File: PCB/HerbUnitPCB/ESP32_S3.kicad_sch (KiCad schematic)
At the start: 12 parts, among them J1 USB_C_Receptacle_USB2.0_16P, U1 USBLC6-2P6, U2 AP2112K-3.3, U3 ESP32-S3-MINI-1

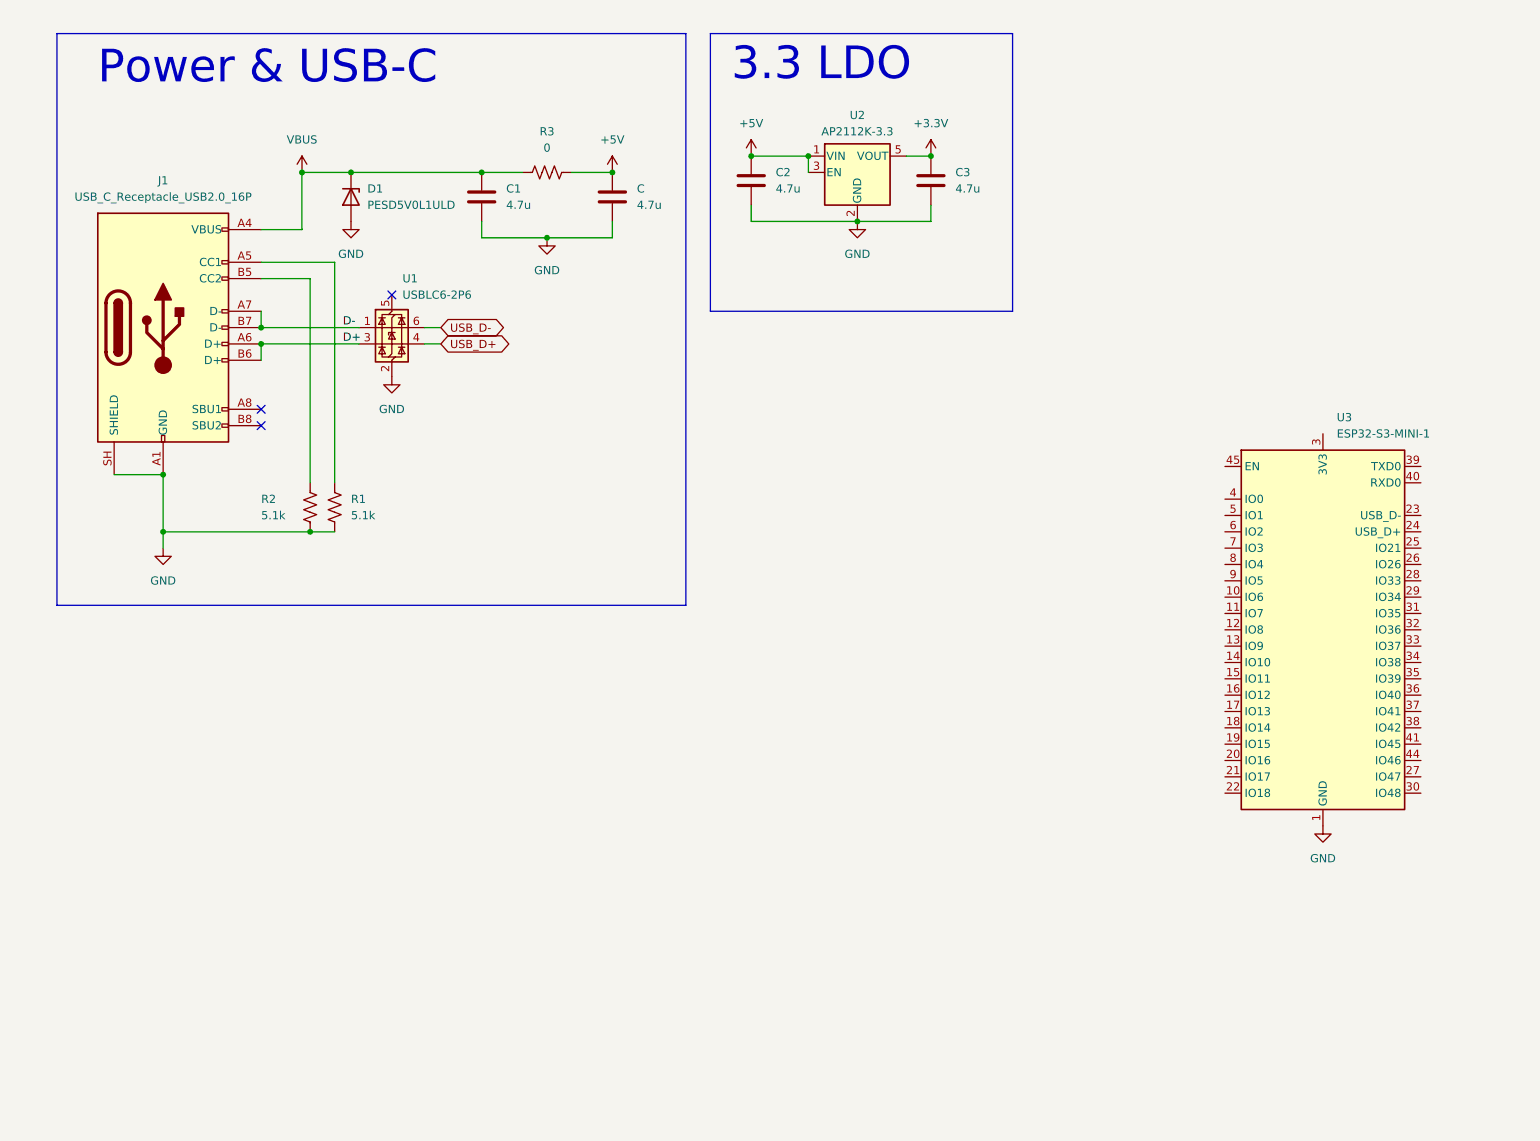
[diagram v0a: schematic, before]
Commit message: Schematic Progress
- Finished ESP Schematic
- Began Peripherals Schematic
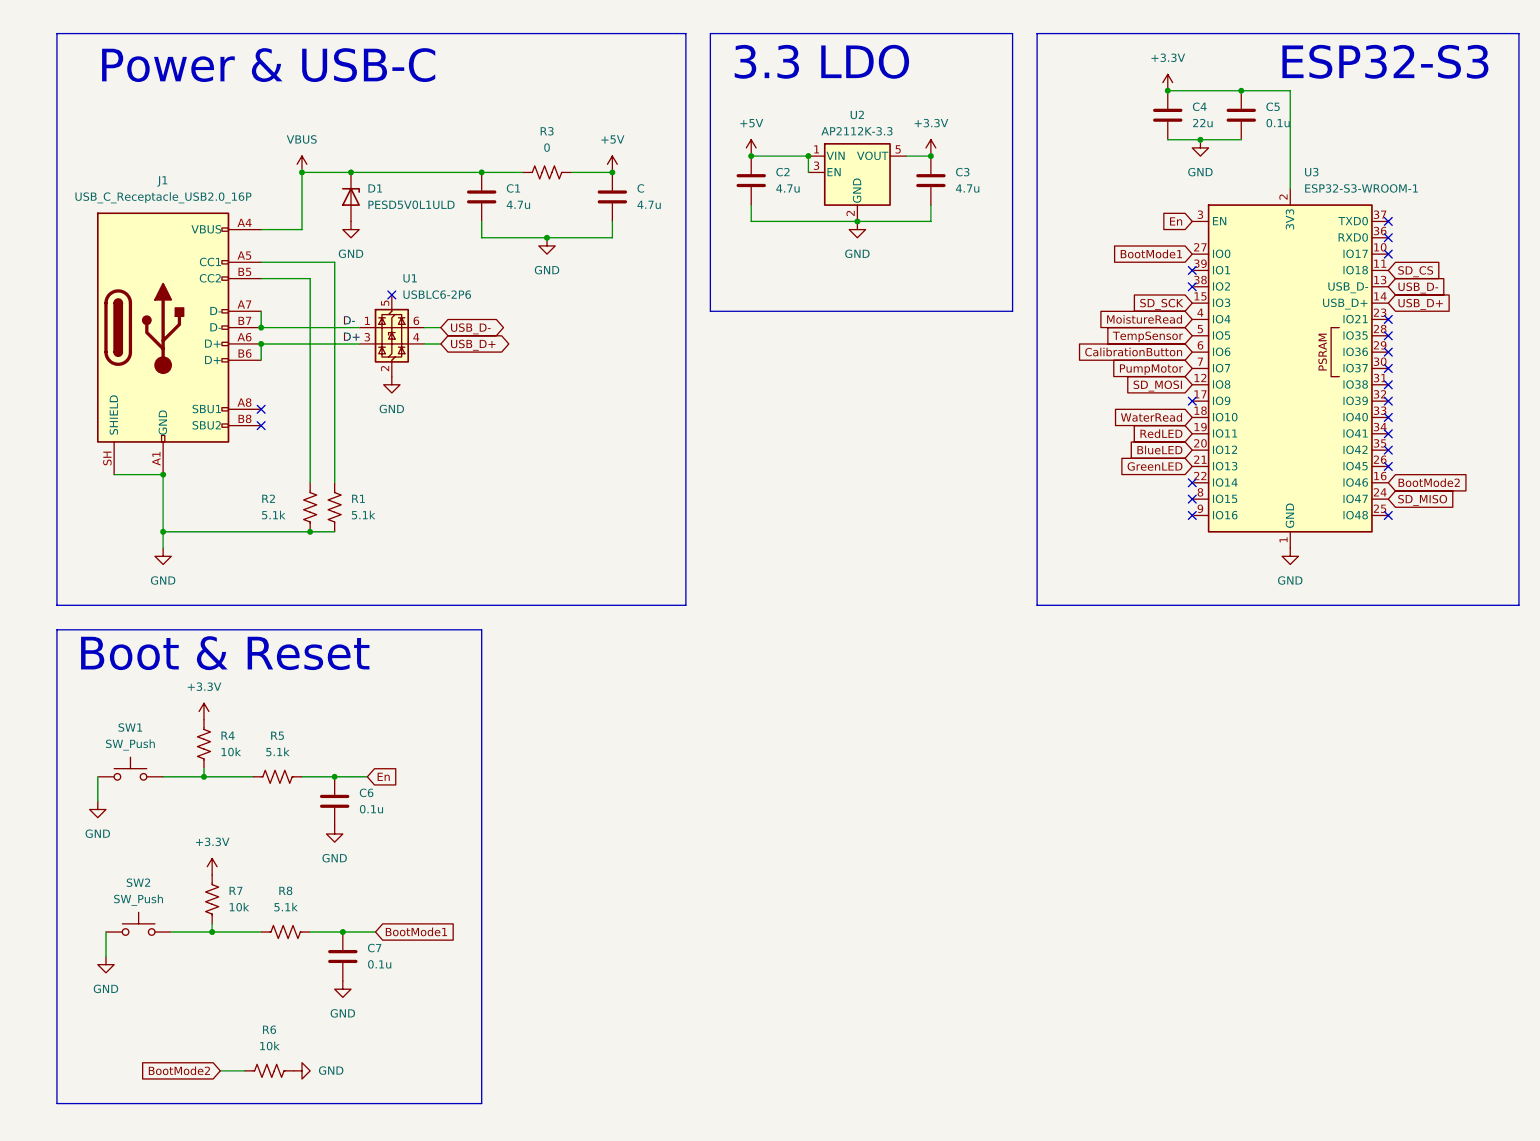
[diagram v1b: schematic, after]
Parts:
- removed U3: ESP32-S3-MINI-1, RF_Module:ESP32-S2-MINI-1, symbol RF_Module:ESP32-S3-MINI-1
- added C4: 22u, Capacitor_SMD:C_0402_1005Metric, symbol Device:C
- added C5, C6, C7: 0.1u, Capacitor_SMD:C_0402_1005Metric, symbol Device:C
- added R4, R6, R7: 10k, Resistor_SMD:R_0402_1005Metric, symbol Device:R_US
- added R5, R8: 5.1k, Resistor_SMD:R_0402_1005Metric, symbol Device:R_US
- added SW1, SW2: SW_Push, Button_Switch_SMD:SW_SPST_B3U-1000P, symbol Switch:SW_Push
- added U3: ESP32-S3-WROOM-1, RF_Module:ESP32-S3-WROOM-1, symbol RF_Module:ESP32-S3-WROOM-1
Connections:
- net +3.3V: now also C4.1, C5.1, R4.1, R7.1, U3.2 (3V3)
- net GND: now also C4.2, C5.2, C6.2, C7.2, R6.2, SW1.1, SW2.1, U3.1 (GND), U3.40 (GND), U3.41 (GND)
- net USB_D+: now also U3.14 (USB_D+)
- net USB_D-: now also U3.13 (USB_D-)
- new net: R7.2, R8.1, SW2.2
- new net: R4.2, R5.1, SW1.2
- new net BlueLED: U3.20 (IO12)
- new net BootMode1: C7.1, R8.2, U3.27 (IO0)
- new net BootMode2: R6.1, U3.16 (IO46)
- new net CalibrationButton: U3.6 (IO6)
- new net En: C6.1, R5.2, U3.3 (EN)
- new net GreenLED: U3.21 (IO13)
- new net MoistureRead: U3.4 (IO4)
- new net PumpMotor: U3.7 (IO7)
- new net RedLED: U3.19 (IO11)
- new net SD_CS: U3.11 (IO18)
- new net SD_MISO: U3.24 (IO47)
- new net SD_MOSI: U3.12 (IO8)
- new net SD_SCK: U3.15 (IO3)
- new net TempSensor: U3.5 (IO5)
- new net WaterRead: U3.18 (IO10)
- no-connect marks 3 -> 23
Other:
- note added: "Boot & Reset"
- note added: "ESP32-S3"

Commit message: Peripherals
Finished most of the Peripherals.
- Added temp sensor
- Added Moisture sensor
- Added float switch
- Added SD card reader/writer
- Still need to add barrel jack/pump
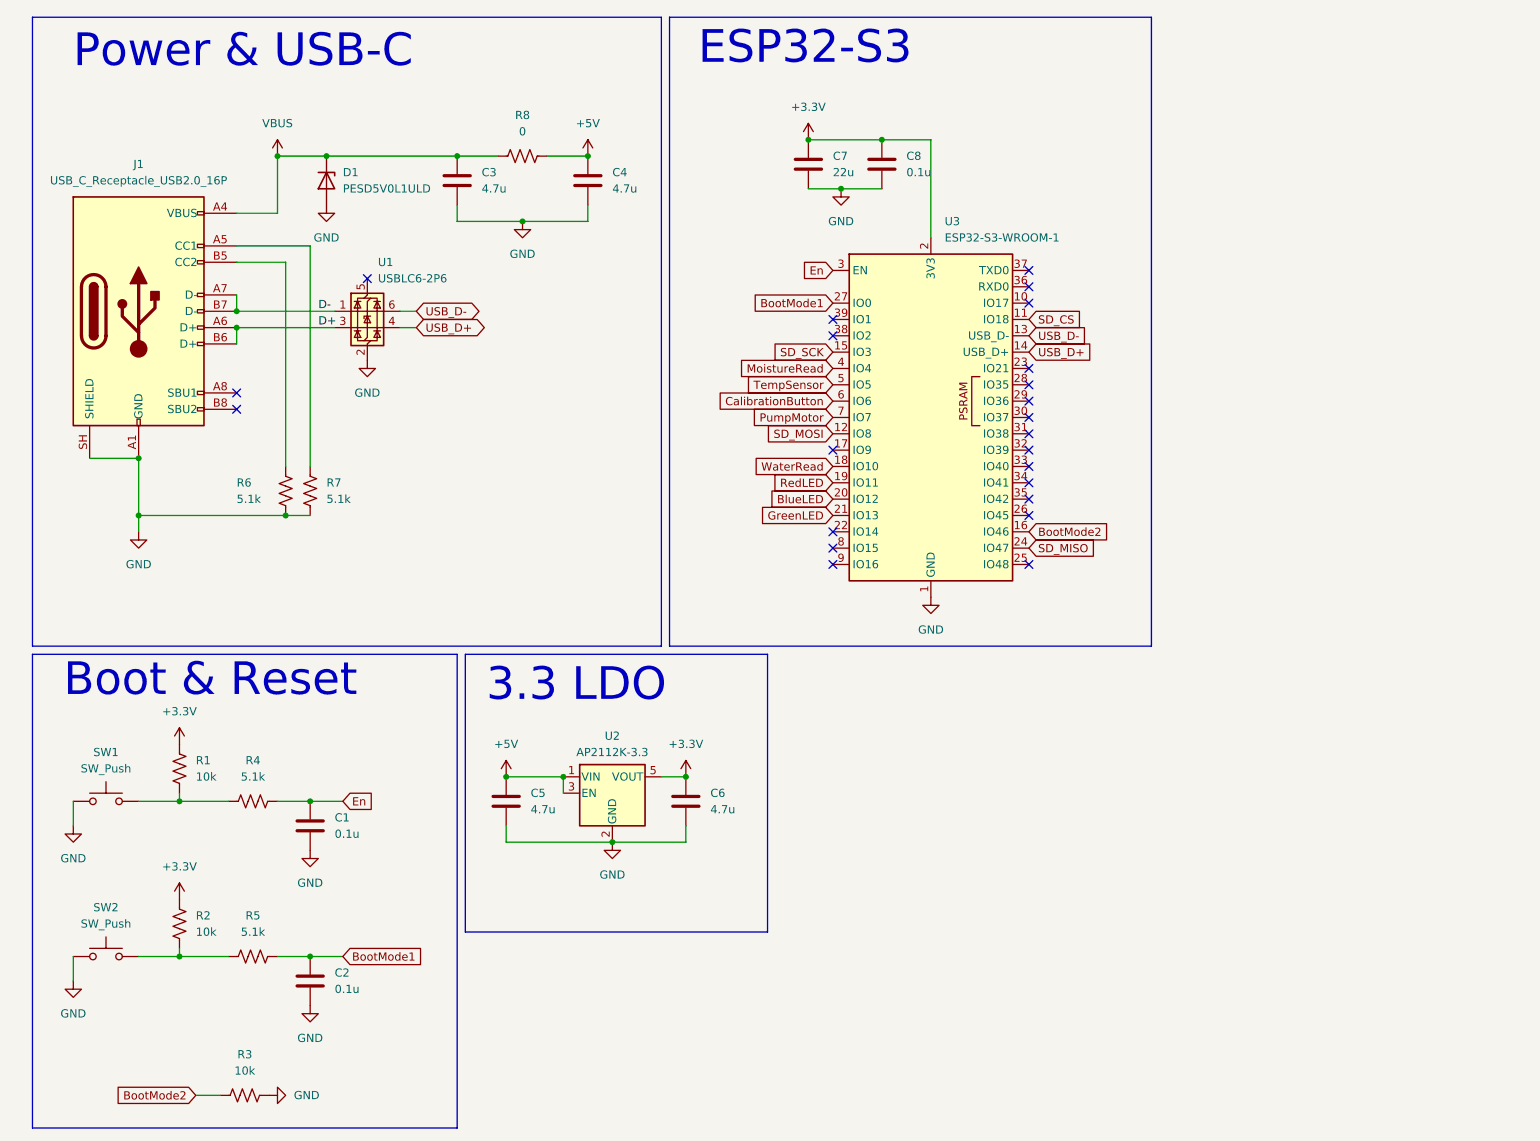
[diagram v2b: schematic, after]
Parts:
- renumbered C6 to C1, C7 to C2, C1 to C3, C to C4, C2 to C5, C3 to C6, C4 to C7, C5 to C8, R4 to R1, R7 to R2, R6 to R3, R5 to R4, R8 to R5, R2 to R6, R1 to R7, R3 to R8
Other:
- moved on the sheet: C1, C2, C3, C4, C5, C6, C7, C8, D1, J1, R1, R2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
